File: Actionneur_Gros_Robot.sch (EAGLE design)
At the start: 27 parts, among them M1 ARDUINO-NANO-3.0#ISP, M10 SERVO, M11 SERVO, M2 SERVO, M3 SERVO, M4 SERVO, M5 SERVO, M6 SERVO, M7 SERVO, M8 SERVO, M9 SERVO

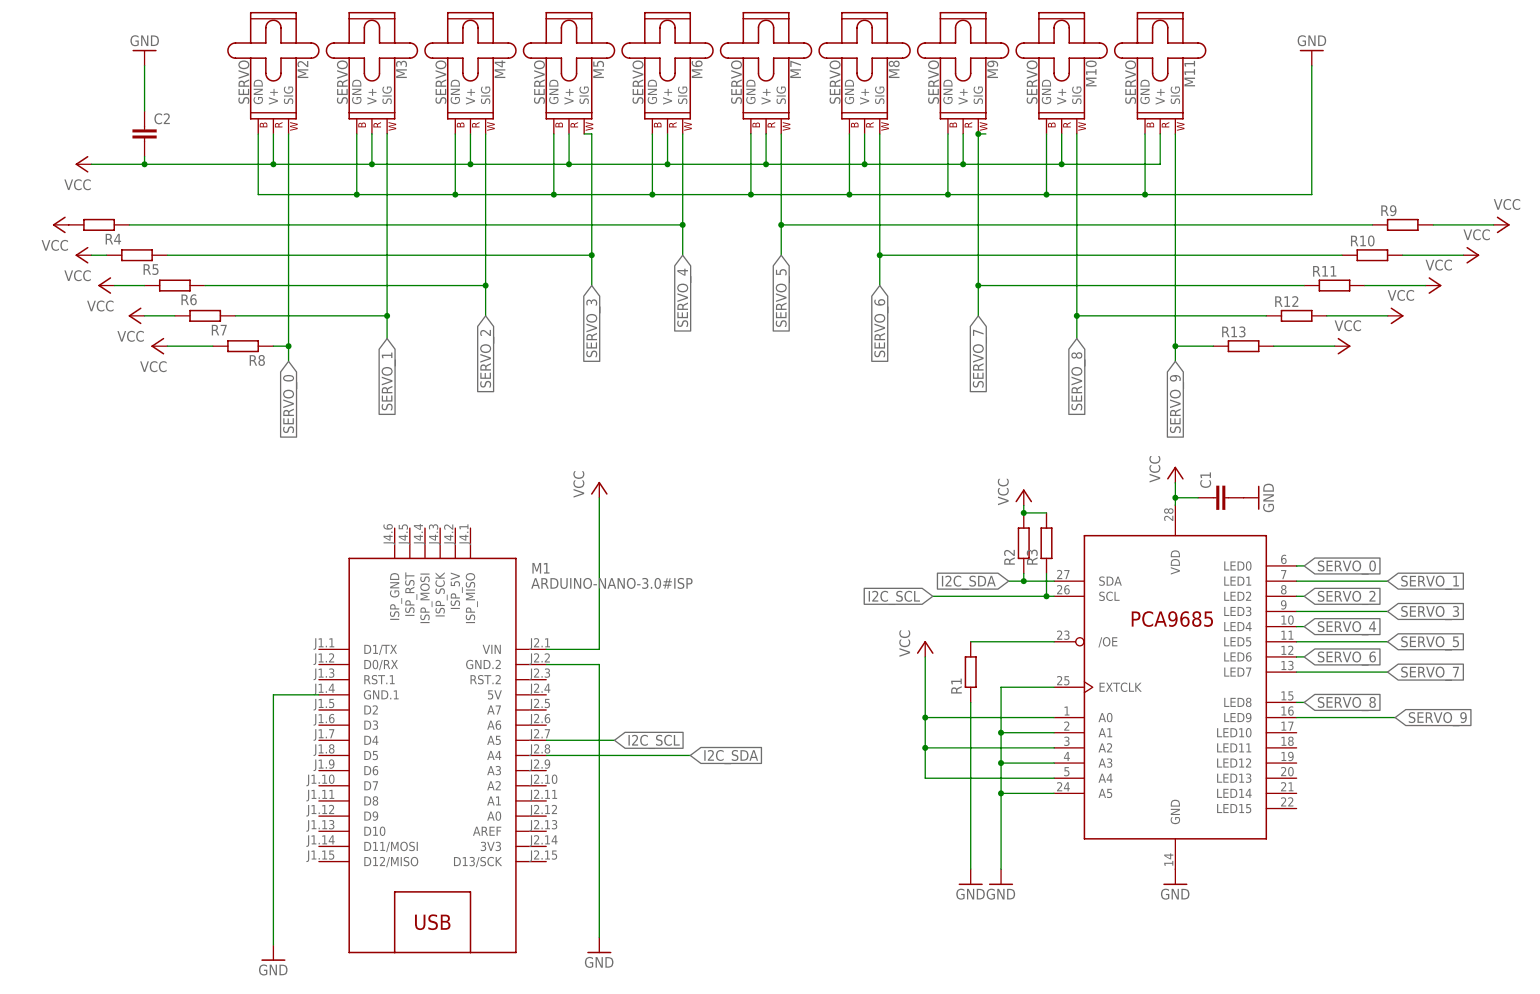
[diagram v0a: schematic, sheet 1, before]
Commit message: added MCP2551 and MCP 2515
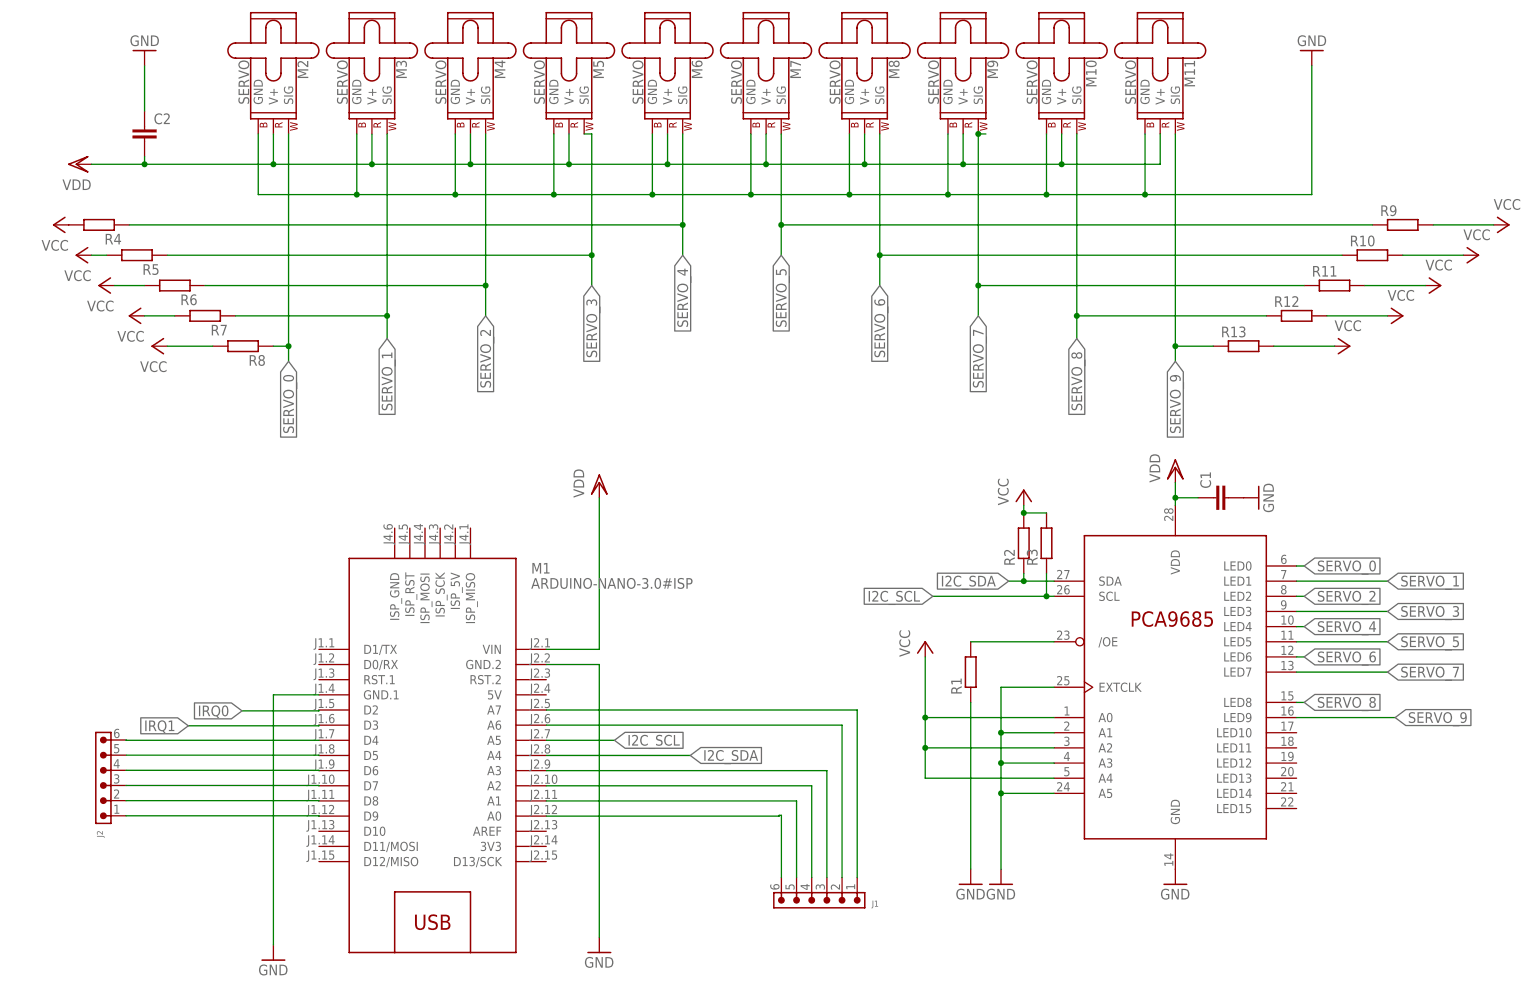
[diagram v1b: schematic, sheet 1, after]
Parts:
- added C3, C4: (no value), rcl:C-EU025-025X050
- added IC1: MCP2515-I_P, MCP2515-I_P:MCP2515-I_P
- added J1, J2: (no value), Wurth_Connectors_WR-PHD:6200XX11121_62000611121
- added J3: (no value), Wurth_Connectors_WR-PHD:6130XX21021_61303221021
- added LED1, LED2: (no value), led:LED3MM
- added R14, R15: (no value), rcl:R-EU_0207/10
- added U$2: MCP2551-I/SN, MCP2551-I_SN:MCP2551-I/SN
- added Y1: 16MHz, Wurth_Quartz Crystals & Oscillators_WE-XTAL:WE-XTAL_HC49_830003231B
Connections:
- new net IRQ0: M1.D2
- new net IRQ1: M1.D3
- new net N$10: J2.3, M1.D7
- new net N$11: J2.4, M1.D6
- new net N$12: J2.5, M1.D5
- new net N$13: J2.6, M1.D4
- new net N$14: C3.2, IC1.OSC2, Y1.2
- new net N$15: C4.2, IC1.OSC1, Y1.1
- new net N$16: LED1.A, R15.1
- new net N$17: LED2.A, R14.1
- new net N$18: IC1.RXCAN, LED2.C
- new net N$19: IC1.TXCAN, LED1.C
- new net N$2: J1.6, M1.A0
- new net N$3: J1.5, M1.A1
- new net N$4: J1.3, M1.A3
- new net N$5: J1.4, M1.A2
- new net N$6: J1.2, M1.A6
- new net N$7: J1.1, M1.A7
- new net N$8: J2.1, M1.D9
- new net N$9: J2.2, M1.D8
- new net VDD: R14.2, R15.2, U$2.VDD
- net GND: now also C3.1, C4.1, U$2.VSS

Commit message: Routing in progress
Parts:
- added LED3: (no value), led:LED3MM
- added R16: 120R, ___RCL:R-EU_0204/5
- added R17: 680R, ___RCL:R-EU_0204/5
- added S1: 430182043816, Wurth_Switch_WS-TASV:430182043816
- M1: value ARDUINO-NANO-3.0#ISP -> ARDUINO-NANO-3.0; device diy-modules2:ARDUINO-NANO-3.0#ISP -> diy-modules2:ARDUINO-NANO-3.0
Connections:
- removed net N$18: IC1.RXCAN, LED2.C
- removed net N$19: IC1.TXCAN, LED1.C
- new net BAU: J3.32
- new net CANH: J3.26, R16.2, U$2.CANH
- new net CANL: J3.28, R16.1, U$2.CANL
- new net CHIP_SELECT: IC1.!CS, M1.D10
- new net MISO1: IC1.SO, M1.D12/MISO
- new net MOSI1: IC1.SI, M1.D11/MOSI
- new net N$20: LED3.A, R17.1
- new net RESET: IC1.!RESET, M1.RST.1, S1.1
- new net RX_CAN1: IC1.RXCAN, LED2.C, U$2.RXD
- new net SCK1: IC1.SCK, M1.D13/SCK
- new net TX_CAN1: IC1.TXCAN, LED1.C, U$2.TXD
- net GND: now also IC1.VSS, J3.20, R17.2, S1.4
- net VDD: now also IC1.VDD, J3.18, LED3.C

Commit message: v2 en cours de révision
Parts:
- removed IC1: MCP2515-I_P, MCP2515-I_P:MCP2515-I_P
- added C5, C6: 100nF, rcl:C-EU025-025X050
- added JP1: (no value), jumper:JP1E
- added SV1, SV2: (no value), con-lstb:MA04-2
- added SV3, SV4: (no value), con-lstb:MA03-2
- added U$3: MCP2515T-E/SO, MCP2515-I_P:MCP2515T-E/SO
- C1: value (none) -> 100nF; device rcl:C-EUC0805 -> rcl:C-EU025-025X050
- C2: value (none) -> 10uF; device rcl:C-EUC0805 -> rcl:CPOL-EUE2.5-7
- C3, C4: value (none) -> 22pF
- J2: device Wurth_Connectors_WR-PHD:6200XX11121_62000611121 -> con-lstb:MA04-2
- R14, R15: value (none) -> 680R
- R16, R17: device ___RCL:R-EU_0204/5 -> rcl:R-EU_0207/7
- Y1: device Wurth_Quartz Crystals & Oscillators_WE-XTAL:WE-XTAL_HC49_830003231B -> crystal:CRYTALHC49UP
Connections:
- removed net N$15: C4.2, IC1.OSC1, Y1.1
- new net +12V: J3.1, J3.2
- new net N$21: C4.2, U$3.OSC1, Y1.1
- new net N$24: C3.2, U$3.OSC2, Y1.2
- net BAU: now also J3.31, JP1.1
- net CANH: now also J3.25
- net CANL: now also J3.27
- net CHIP_SELECT: now also U$3.~CS; no longer IC1.!CS
- net GND: now also C2.+, C5.2, C6.2, J3.11, J3.12, J3.19, J3.23, J3.24, J3.3, J3.4, J3.7, J3.8, S1.2, SV1.5, SV1.6, SV2.5, SV2.6, SV3.1, SV3.3, SV3.5, SV4.1, SV4.3, SV4.5, U$3.VSS; no longer C2.1, IC1.VSS
- net I2C_SCL: now also SV1.3, SV1.4, SV2.3, SV2.4
- net I2C_SDA: now also SV1.1, SV1.2, SV2.1, SV2.2
- net IRQ0: now also J2.1
- net IRQ1: now also J2.2
- net MISO1: now also U$3.SO; no longer IC1.SO
- net MOSI1: now also U$3.SI; no longer IC1.SI
- net N$10: now also J2.6; no longer J2.3
- net N$11: now also J2.5; no longer J2.4
- net N$12: now also J2.4; no longer J2.5
- net N$13: now also J2.3; no longer J2.6
- net N$14: now also J3.5, J3.6; no longer C3.2, IC1.OSC2, Y1.2
- net N$8: now also J2.8; no longer J2.1
- net N$9: now also J2.7; no longer J2.2
- net RESET: now also U$3.~RESET; no longer IC1.!RESET
- net RX_CAN1: now also LED1.C, U$3.RXCAN; no longer IC1.RXCAN, LED2.C
- net SCK1: now also U$3.SCK; no longer IC1.SCK
- net TX_CAN1: now also LED2.C, U$3.TXCAN; no longer IC1.TXCAN, LED1.C
- net VCC: now also C2.-, J3.21, J3.22, M1.5V, SV4.2, SV4.4, SV4.6; no longer C2.2, M1.VIN
- net VDD: now also C5.1, C6.1, J3.17, JP1.2, SV1.7, SV1.8, SV2.7, SV2.8, SV3.2, SV3.4, SV3.6, U$3.VDD; no longer IC1.VDD
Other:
- moved on the sheet: C3, C4, J2, J3, LED1, LED2, LED3, R14, R15, R17, R4, S1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

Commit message: Ajout des pins 12V
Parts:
- added SV5: (no value), con-lstb:MA03-2
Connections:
- net +12V: now also SV5.2, SV5.4, SV5.6
- net GND: now also SV5.1, SV5.3, SV5.5
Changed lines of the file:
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@@
 <part name="GND21" library="supply1" library_urn="urn:adsk.eagle:library:371" deviceset="GND" device=""/>
 <part name="P+18" library="supply1" library_urn="urn:adsk.eagle:library:371" deviceset="VCC" device=""/>
+<part name="SV5" library="con-lstb" library_urn="urn:adsk.eagle:library:162" deviceset="MA03-2" device="" package3d_urn="urn:adsk.eagle:package:8334/1"/>
+<part name="GND22" library="supply1" library_urn="urn:adsk.eagle:library:371" deviceset="GND" device=""/>
+<part name="P+19" library="supply1" library_urn="urn:adsk.eagle:library:371" deviceset="+12V" device=""/>
 </parts>
 <sheets>
@@
 <attribute name="VALUE" x="77.47" y="118.872" size="1.778" layer="96" rot="R90"/>
 </instance>
+<instance part="SV5" gate="1" x="135.636" y="128.27" smashed="yes">
+<attribute name="VALUE" x="131.826" y="120.65" size="1.778" layer="96"/>
+<attribute name="NAME" x="131.826" y="134.112" size="1.778" layer="95"/>
+</instance>
+<instance part="GND22" gate="1" x="154.178" y="122.936" smashed="yes">
+<attribute name="VALUE" x="151.638" y="120.396" size="1.778" layer="96"/>
+</instance>
+<instance part="P+19" gate="1" x="122.936" y="137.922" smashed="yes">
+<attribute name="VALUE" x="120.396" y="132.842" size="1.778" layer="96" rot="R90"/>
+</instance>
 </instances>
 <busses>
@@
 <wire x1="101.346" y1="113.284" x2="112.268" y2="113.284" width="0.1524" layer="91"/>
 </segment>
+<segment>
+<pinref part="GND22" gate="1" pin="GND"/>
+<wire x1="154.178" y1="125.476" x2="154.178" y2="128.27" width="0.1524" layer="91"/>
+<pinref part="SV5" gate="1" pin="5"/>
+<pinref part="SV5" gate="1" pin="3"/>
+<wire x1="143.256" y1="130.81" x2="143.256" y2="128.27" width="0.1524" layer="91"/>
+<pinref part="SV5" gate="1" pin="1"/>
+<wire x1="143.256" y1="128.27" x2="143.256" y2="125.73" width="0.1524" layer="91"/>
+<junction x="143.256" y="128.27"/>
+<wire x1="143.256" y1="128.27" x2="154.178" y2="128.27" width="0.1524" layer="91"/>
+</segment>
 </net>
 <net name="VDD" class="0">
@@
 <junction x="40.42" y="62.78"/>
 </segment>
-</net>
+<segment>
+<pinref part="P+19" gate="1" pin="+12V"/>
+<pinref part="SV5" gate="1" pin="6"/>
+<wire x1="122.936" y1="135.382" x2="122.936" y2="130.81" width="0.1524" layer="91"/>
+<wire x1="122.936" y1="130.81" x2="128.016" y2="130.81" width="0.1524" layer="91"/>
+<pinref part="SV5" gate="1" pin="4"/>
+<wire x1="128.016" y1="130.81" x2="128.016" y2="128.27" width="0.1524" layer="91"/>
+<junction x="128.016" y="130.81"/>
+<pinref part="SV5" gate="1" pin="2"/>
+<wire x1="128.016" y1="125.73" x2="128.016" y2="128.27" width="0.1524" layer="91"/>
+<junction x="128.016" y="128.27"/>
+</segment>
+</net>

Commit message: chgt schéma bouton d'arrêt d'urgence, condo 10 uF sur VDD
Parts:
- added R18: 10K, rcl:R-EU_0207/7
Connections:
- net BAU: now also JP1.2, R18.1; no longer JP1.1
- net GND: now also JP1.1
- net VCC: now also R18.2
- net VDD: no longer JP1.2
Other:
- note added: "tourner le 12V"
- moved on the sheet: JP1
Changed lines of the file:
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@@
 <part name="GND12" library="supply1" library_urn="urn:adsk.eagle:library:371" deviceset="GND" device=""/>
 <part name="JP1" library="jumper" library_urn="urn:adsk.eagle:library:252" deviceset="JP1E" device="" package3d_urn="urn:adsk.eagle:package:15455/1"/>
-<part name="VDD6" library="supply1" library_urn="urn:adsk.eagle:library:371" deviceset="VDD" device=""/>
 <part name="SV1" library="con-lstb" library_urn="urn:adsk.eagle:library:162" deviceset="MA04-2" device="" package3d_urn="urn:adsk.eagle:package:8368/1"/>
 <part name="VDD7" library="supply1" library_urn="urn:adsk.eagle:library:371" deviceset="VDD" device=""/>
@@
 <part name="GND22" library="supply1" library_urn="urn:adsk.eagle:library:371" deviceset="GND" device=""/>
 <part name="P+19" library="supply1" library_urn="urn:adsk.eagle:library:371" deviceset="+12V" device=""/>
+<part name="GND23" library="supply1" library_urn="urn:adsk.eagle:library:371" deviceset="GND" device=""/>
+<part name="R18" library="rcl" library_urn="urn:adsk.eagle:library:334" deviceset="R-EU_" device="0207/7" package3d_urn="urn:adsk.eagle:package:23493/2" value="10K"/>
+<part name="P+20" library="supply1" library_urn="urn:adsk.eagle:library:371" deviceset="VCC" device=""/>
 </parts>
 <sheets>
@@
 <wire x1="196.85" y1="148.59" x2="180.34" y2="148.59" width="0.1524" layer="91"/>
 <junction x="180.34" y="148.59"/>
+<pinref part="C2" gate="G$1" pin="-"/>
+<wire x1="26.67" y1="153.67" x2="26.67" y2="148.59" width="0.1524" layer="91"/>
+<wire x1="26.67" y1="148.59" x2="17.78" y2="148.59" width="0.1524" layer="91"/>
+<junction x="17.78" y="148.59"/>
 </segment>
 <segment>
 <pinref part="P+6" gate="VCC" pin="VCC"/>
 <pinref part="R4" gate="G$1" pin="2"/>
-<wire x1="11.176" y1="138.43" x2="26.67" y2="138.43" width="0.1524" layer="91"/>
-<pinref part="C2" gate="G$1" pin="-"/>
-<wire x1="26.67" y1="138.43" x2="33.274" y2="138.43" width="0.1524" layer="91"/>
-<wire x1="26.67" y1="153.67" x2="26.67" y2="138.43" width="0.1524" layer="91"/>
-<junction x="26.67" y="138.43"/>
+<wire x1="11.176" y1="138.43" x2="33.274" y2="138.43" width="0.1524" layer="91"/>
 </segment>
 <segment>
@@
 <description>CAN AND STEPPER MOTORS</description>
 <plain>
+<text x="128.27" y="118.872" size="1.778" layer="91">tourner le 12V</text>
 </plain>
 <instances>
@@
 <attribute name="VALUE" x="23.96" y="43.96" size="1.778" layer="96" rot="R90"/>
 </instance>
-<instance part="GND13" gate="1" x="26.5" y="16" smashed="yes">
-<attribute name="VALUE" x="23.96" y="13.46" size="1.778" layer="96"/>
+<instance part="GND13" gate="1" x="34.628" y="15.746" smashed="yes">
+<attribute name="VALUE" x="32.088" y="13.206" size="1.778" layer="96"/>
 </instance>
 <instance part="R16" gate="G$1" x="91.5" y="36.5" smashed="yes" rot="R90">
@@
 <attribute name="VALUE" x="219.46" y="52.96" size="1.778" layer="96"/>
 </instance>
-<instance part="JP1" gate="A" x="19.5" y="76.5" smashed="yes">
-<attribute name="NAME" x="18.23" y="76.5" size="1.778" layer="95" rot="R90"/>
-<attribute name="VALUE" x="25.215" y="76.5" size="1.778" layer="96" rot="R90"/>
-</instance>
-<instance part="VDD6" gate="G$1" x="31" y="90.5" smashed="yes">
-<attribute name="VALUE" x="28.46" y="87.96" size="1.778" layer="96" rot="R90"/>
+<instance part="JP1" gate="A" x="15.436" y="28.24" smashed="yes">
+<attribute name="NAME" x="14.166" y="28.24" size="1.778" layer="95" rot="R90"/>
+<attribute name="VALUE" x="21.151" y="28.24" size="1.778" layer="96" rot="R90"/>
 </instance>
 <instance part="SV1" gate="G$1" x="40.894" y="145.542" smashed="yes">
@@
 <instance part="P+19" gate="1" x="122.936" y="137.922" smashed="yes">
 <attribute name="VALUE" x="120.396" y="132.842" size="1.778" layer="96" rot="R90"/>
+</instance>
+<instance part="GND23" gate="1" x="15.324" y="17.27" smashed="yes">
+<attribute name="VALUE" x="12.784" y="14.73" size="1.778" layer="96"/>
+</instance>
+<instance part="R18" gate="G$1" x="12.332" y="39.502" smashed="yes" rot="R90">
+<attribute name="NAME" x="10.8334" y="35.692" size="1.778" layer="95" rot="R90"/>
+<attribute name="VALUE" x="15.634" y="35.692" size="1.778" layer="96" rot="R90"/>
+</instance>
+<instance part="P+20" gate="VCC" x="12.446" y="61.722" smashed="yes">
+<attribute name="VALUE" x="9.906" y="59.182" size="1.778" layer="96" rot="R90"/>
 </instance>
 </instances>
@@
 <pinref part="GND13" gate="1" pin="GND"/>
 <pinref part="J3" gate="G$1" pin="20"/>
-<wire x1="26.5" y1="18.54" x2="26.5" y2="39.92" width="0.1524" layer="91"/>
-<wire x1="26.5" y1="39.92" x2="40.42" y2="39.92" width="0.1524" layer="91"/>
+<wire x1="34.628" y1="18.286" x2="34.628" y2="39.92" width="0.1524" layer="91"/>
+<wire x1="34.628" y1="39.92" x2="40.42" y2="39.92" width="0.1524" layer="91"/>
 <pinref part="J3" gate="G$1" pin="19"/>
 <wire x1="40.42" y1="39.92" x2="50.58" y2="39.92" width="0.1524" layer="91"/>
@@
 <wire x1="58.42" y1="50.08" x2="58.42" y2="39.92" width="0.1524" layer="91"/>
 <junction x="50.58" y="50.08"/>
-<wire x1="58.42" y1="39.878" x2="58.42" y2="39.92" width="0.1524" layer="91"/>
 <wire x1="58.42" y1="39.92" x2="50.58" y2="39.92" width="0.1524" layer="91"/>
 <junction x="50.58" y="39.92"/>
 <pinref part="J3" gate="G$1" pin="23"/>
-<wire x1="58.42" y1="39.878" x2="58.42" y2="34.84" width="0.1524" layer="91"/>
+<wire x1="58.42" y1="39.92" x2="58.42" y2="34.84" width="0.1524" layer="91"/>
 <wire x1="58.42" y1="34.84" x2="50.58" y2="34.84" width="0.1524" layer="91"/>
 <pinref part="J3" gate="G$1" pin="24"/>
@@
 <wire x1="143.256" y1="128.27" x2="154.178" y2="128.27" width="0.1524" layer="91"/>
 </segment>
+<segment>
+<pinref part="JP1" gate="A" pin="1"/>
+<pinref part="GND23" gate="1" pin="GND"/>
+<wire x1="15.436" y1="25.7" x2="15.436" y2="22.096" width="0.1524" layer="91"/>
+<wire x1="15.436" y1="22.096" x2="15.324" y2="19.81" width="0.1524" layer="91"/>
+</segment>
 </net>
 <net name="VDD" class="0">
@@
 <wire x1="217.36" y1="81.8" x2="229" y2="81.8" width="0.1524" layer="91"/>
 <wire x1="229" y1="81.8" x2="229" y2="135.46" width="0.1524" layer="91"/>
-</segment>
-<segment>
-<pinref part="VDD6" gate="G$1" pin="VDD"/>
-<pinref part="JP1" gate="A" pin="2"/>
-<wire x1="31" y1="73.96" x2="31" y2="87.96" width="0.1524" layer="91"/>
-<wire x1="22.04" y1="73.96" x2="31" y2="73.96" width="0.1524" layer="91"/>
 </segment>
 <segment>
@@
 <segment>
 <pinref part="J3" gate="G$1" pin="26"/>
-<wire x1="40.42" y1="32.3" x2="23.5" y2="32.3" width="0.1524" layer="91"/>
-<wire x1="23.5" y1="32.3" x2="23.5" y2="33.5" width="0.1524" layer="91"/>
-<label x="23.5" y="33.5" size="1.778" layer="95" rot="R180" xref="yes"/>
+<wire x1="40.42" y1="32.3" x2="31.12" y2="32.3" width="0.1524" layer="91"/>
+<wire x1="31.12" y1="32.3" x2="31.12" y2="34.77" width="0.1524" layer="91"/>
+<label x="31.12" y="34.77" size="1.778" layer="95" rot="R180" xref="yes"/>
 <pinref part="J3" gate="G$1" pin="25"/>
 <wire x1="40.42" y1="32.3" x2="50.58" y2="32.3" width="0.1524" layer="91"/>
@@
 <pinref part="J3" gate="G$1" pin="28"/>
 <wire x1="40.42" y1="29.76" x2="40.42" y2="29.5" width="0.1524" layer="91"/>
-<wire x1="40.42" y1="29.5" x2="24" y2="29.5" width="0.1524" layer="91"/>
-<label x="24" y="29.5" size="1.778" layer="95" rot="R180" xref="yes"/>
+<wire x1="40.42" y1="29.5" x2="31.112" y2="29.5" width="0.1524" layer="91"/>
+<label x="31.112" y="29.5" size="1.778" layer="95" rot="R180" xref="yes"/>
 <pinref part="J3" gate="G$1" pin="27"/>
 <wire x1="40.42" y1="29.76" x2="50.58" y2="29.76" width="0.1524" layer="91"/>
@@
 <pinref part="J3" gate="G$1" pin="31"/>
 <wire x1="40.42" y1="24.68" x2="50.58" y2="24.68" width="0.1524" layer="91"/>
-<wire x1="40.42" y1="24.68" x2="9" y2="24.68" width="0.1524" layer="91"/>
-<wire x1="9" y1="24.68" x2="9" y2="73.96" width="0.1524" layer="91"/>
-<junction x="40.42" y="24.68"/>
-<pinref part="JP1" gate="A" pin="1"/>
-<wire x1="9" y1="73.96" x2="19.5" y2="73.96" width="0.1524" layer="91"/>
 <wire x1="50.58" y1="24.68" x2="50.58" y2="24.638" width="0.1524" layer="91"/>
 <wire x1="50.58" y1="24.638" x2="54.102" y2="24.638" width="0.1524" layer="91"/>
 <junction x="50.58" y="24.68"/>
 <label x="54.102" y="24.638" size="1.778" layer="95" xref="yes"/>
+<pinref part="JP1" gate="A" pin="2"/>
+<wire x1="40.42" y1="24.68" x2="17.976" y2="24.68" width="0.1524" layer="91"/>
+<wire x1="17.976" y1="24.68" x2="17.976" y2="25.7" width="0.1524" layer="91"/>
+<junction x="40.42" y="24.68"/>
+<pinref part="R18" gate="G$1" pin="1"/>
+<wire x1="12.332" y1="34.422" x2="20.828" y2="34.422" width="0.1524" layer="91"/>
+<wire x1="20.828" y1="34.422" x2="20.828" y2="25.7" width="0.1524" layer="91"/>
+<wire x1="20.828" y1="25.7" x2="17.976" y2="25.7" width="0.1524" layer="91"/>
+<junction x="17.976" y="25.7"/>
 </segment>
 </net>
@@
 <junction x="80.01" y="113.284"/>
 </segment>
-</net>
+<segment>
+<pinref part="P+20" gate="VCC" pin="VCC"/>
+<pinref part="R18" gate="G$1" pin="2"/>
+<wire x1="12.446" y1="59.182" x2="12.332" y2="59.182" width="0.1524" layer="91"/>
+<wire x1="12.332" y1="59.182" x2="12.332" y2="44.582" width="0.1524" layer="91"/>
+</segment>
+</net>
